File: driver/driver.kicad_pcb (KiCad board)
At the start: 2 copper layers, 100 x 100 mm, 103 parts, among them J1 OUT_A, J10 FAN, J2 OUT_B, J4 RJ45_LED_Shielded, J5 RJ45_LED_Shielded, J6 1602 I2C LCD, J7 IN_VCC, J8 IN_GND, J9 SWD, Q1 TPHR6503PL, Q2 TPHR6503PL, Q3 TPHR6503PL, Q4 TPHR6503PL, U1 MT3608, U10 PC817, U11 AMS1117-5.0, U12 PC817, U13 MAX485E, U2 74HC595, U3 AMS1117-3.3, U4 TC4427, U5 TC4427, U6 STM32F030F4Px, U7 INA226, U8 MCP9804_MSOP, U9 PC817, Y1 8MHz

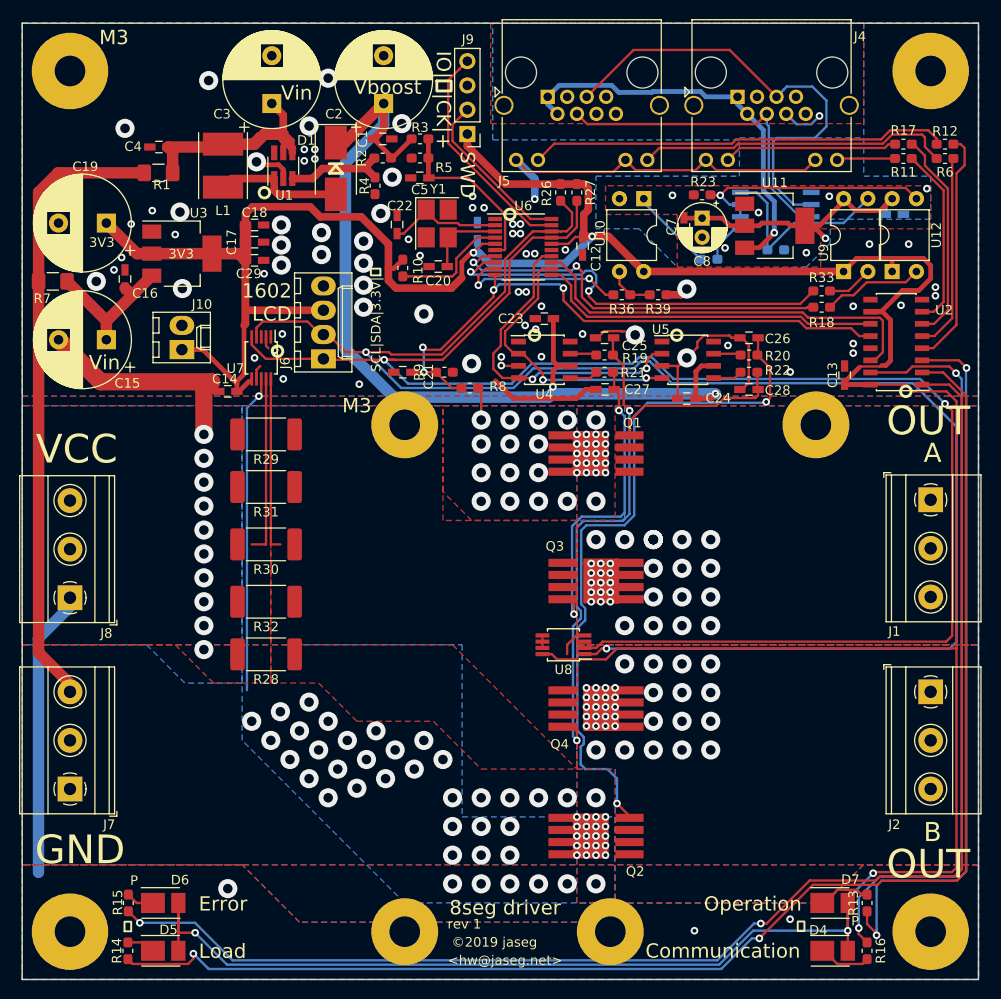
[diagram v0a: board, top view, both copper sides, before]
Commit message: driver: fix a few misplaced vias, set grid origin, fix bottom mask
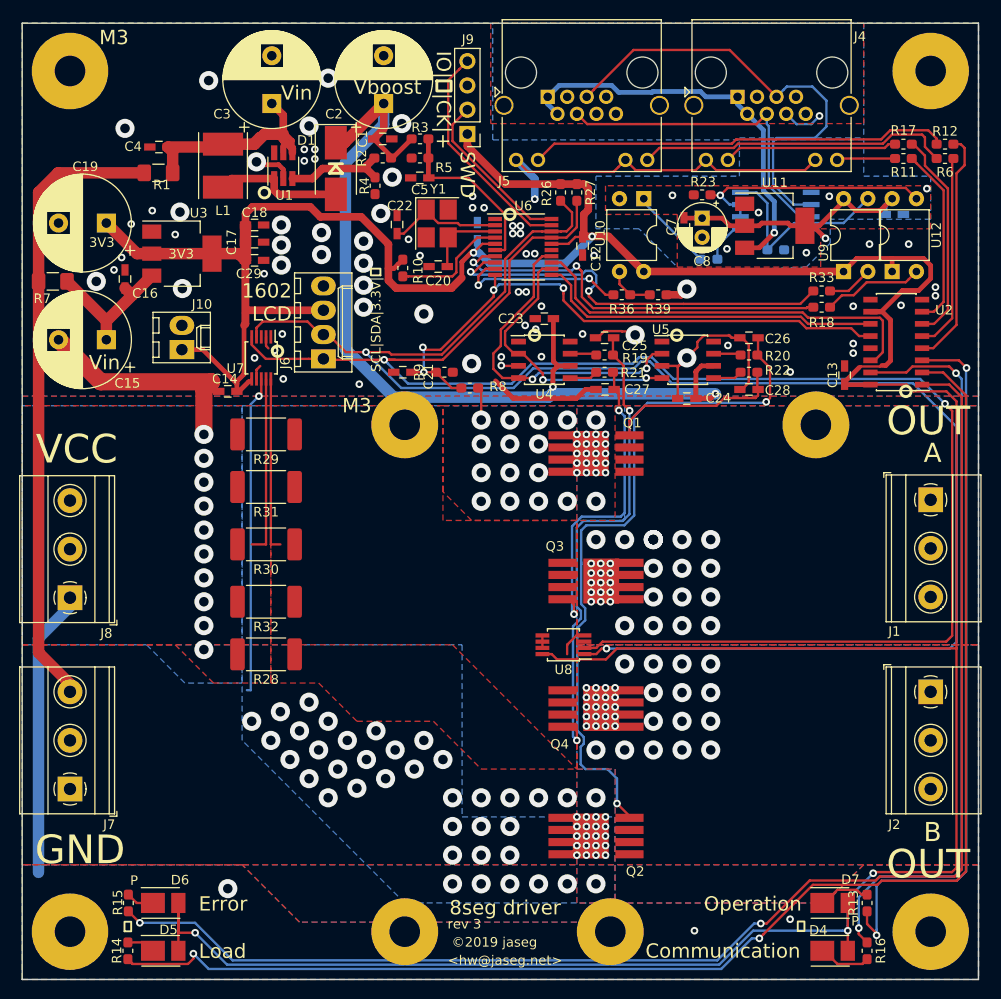
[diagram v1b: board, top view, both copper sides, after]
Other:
- board text added: "rev 3"
- board text removed: "rev 1"
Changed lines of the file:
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@@
     (thickness 1.6)
     (drawings 126)
-    (tracks 1099)
+    (tracks 1100)
     (zones 0)
     (modules 103)
@@
     (user_trace_width 3.2)
     (trace_clearance 0.2)
-    (zone_clearance 0.25)
+    (zone_clearance 0.3)
     (zone_45_only no)
     (trace_min 0.15)
@@
     (solder_mask_min_width 0.25)
     (aux_axis_origin 0 0)
+    (grid_origin 70 55)
     (visible_elements FFFFFF7F)
     (pcbplotparams
-      (layerselection 0x010fc_ffffffff)
+      (layerselection 0x011fc_ffffffff)
       (usegerberextensions false)
       (usegerberattributes false)
@@
       (padsonsilk false)
       (subtractmaskfromsilk false)
-      (outputformat 1)
+      (outputformat 5)
       (mirror false)
-      (drillshape 0)
+      (drillshape 1)
       (scaleselection 1)
-      (outputdirectory "gerber"))
+      (outputdirectory "render"))
   )
   (net 0 "")
@@
   (gr_line (start 90.5 128) (end 79.5 124) (layer B.Mask) (width 2.5))
   (gr_line (start 158 99) (end 165 99) (layer B.Mask) (width 2.5))
-  (gr_text "rev 1" (at 116.238095 149.21) (layer F.SilkS)
+  (gr_text "rev 3" (at 116.238095 149.21) (layer F.SilkS)
     (effects (font (size 1 1) (thickness 0.2)))
   )
@@
   (gr_poly (pts (xy 143 121) (xy 143 132) (xy 129 132) (xy 129 121)) (layer B.Mask) (width 0.15))
   (gr_poly (pts (xy 131.5 106) (xy 131.5 95) (xy 116.5 95) (xy 116.5 106)) (layer B.Mask) (width 0.15))
-  (gr_poly (pts (xy 129 108) (xy 143 108) (xy 143 119) (xy 129 119)) (layer B.Mask) (width 0.15))
+  (gr_poly (pts (xy 129.3 108) (xy 143 108) (xy 143 119) (xy 129.3 119)) (layer B.Mask) (width 0.15))
   (gr_poly (pts (xy 138 121) (xy 143 121) (xy 143 132) (xy 138 132)) (layer F.Mask) (width 0.15))
   (gr_poly (pts (xy 138 109) (xy 142.5 109) (xy 143 109) (xy 143 119) (xy 138 119)) (layer F.Mask) (width 0.15))
@@
   )
   (dimension 5 (width 0.3) (layer Dwgs.User)
-    (gr_text "5.000 mm" (at 62.9 57.5 90) (layer Dwgs.User)
+    (gr_text "5.000 mm" (at 62.9 62 90) (layer Dwgs.User)
       (effects (font (size 1.5 1.5) (thickness 0.3)))
     )
@@
   )
   (dimension 35 (width 0.3) (layer Dwgs.User)
-    (gr_text "35.000 mm" (at 62.9 137.5 90) (layer Dwgs.User)
+    (gr_text "35.000 mm" (at 62.9 130 90) (layer Dwgs.User)
       (effects (font (size 1.5 1.5) (thickness 0.3)))
     )
@@
   (via (at 110.4 77.6) (size 0.8) (drill 0.4) (layers F.Cu B.Cu) (net 2))
   (via (at 111.6 79.3) (size 0.8) (drill 0.4) (layers F.Cu B.Cu) (net 2))
-  (via (at 126.8 78.7) (size 0.8) (drill 0.4) (layers F.Cu B.Cu) (net 2))
-  (via (at 121.3 76) (size 0.8) (drill 0.4) (layers F.Cu B.Cu) (net 2))
-  (via (at 122.1 76) (size 0.8) (drill 0.4) (layers F.Cu B.Cu) (net 2))
+  (via (at 129.8 79.3) (size 0.8) (drill 0.4) (layers F.Cu B.Cu) (net 2))
+  (via (at 121.3 76.2) (size 0.8) (drill 0.4) (layers F.Cu B.Cu) (net 2))
+  (via (at 122.1 76.2) (size 0.8) (drill 0.4) (layers F.Cu B.Cu) (net 2))
   (via (at 121.3 77) (size 0.8) (drill 0.4) (layers F.Cu B.Cu) (net 2))
   (via (at 122.1 77) (size 0.8) (drill 0.4) (layers F.Cu B.Cu) (net 2))
@@
   (via (at 152 79) (size 0.8) (drill 0.4) (layers F.Cu B.Cu) (net 10))
   (via (at 138 73) (size 0.8) (drill 0.4) (layers F.Cu B.Cu) (net 10))
-  (via (at 143.5 78.5) (size 0.8) (drill 0.4) (layers F.Cu B.Cu) (net 10))
+  (via (at 143.7 78.6) (size 0.8) (drill 0.4) (layers F.Cu B.Cu) (net 10))
   (via (at 147 74.8) (size 0.8) (drill 0.4) (layers F.Cu B.Cu) (net 10))
   (via (at 154.4 73.1) (size 0.8) (drill 0.4) (layers F.Cu B.Cu) (net 10))
@@
   (segment (start 95 92.2) (end 95 93.75) (width 0.25) (layer F.Cu) (net 21))
   (segment (start 95 93.75) (end 94.75 94) (width 0.25) (layer F.Cu) (net 21))
-  (segment (start 94.75 94) (end 93.5 95.25) (width 0.25) (layer B.Cu) (net 21))
-  (segment (start 93.5 95.25) (end 93.5 124.75) (width 0.25) (layer B.Cu) (net 21))
   (segment (start 73.75 70.65) (end 82.7625 70.65) (width 1.2) (layer F.Cu) (net 21))
   (segment (start 71.7125 72.6875) (end 73.75 70.65) (width 1.2) (layer F.Cu) (net 21))
@@
   (segment (start 118 93.475) (end 117.675 93.15) (width 0.25) (layer F.Cu) (net 21))
   (segment (start 118 96.5) (end 118 93.475) (width 0.25) (layer F.Cu) (net 21))
+  (segment (start 93.9 124.75) (end 93.5 124.75) (width 0.25) (layer B.Cu) (net 21))
+  (segment (start 94.75 94) (end 93.9 94.85) (width 0.25) (layer B.Cu) (net 21))
+  (segment (start 93.9 94.85) (end 93.9 124.75) (width 0.25) (layer B.Cu) (net 21))
   (segment (start 96 92.2) (end 96 109.5) (width 0.25) (layer F.Cu) (net 22))
   (segment (start 96 109.5) (end 97 109.5) (width 0.25) (layer F.Cu) (net 22))

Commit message: driver: Fix ALL the PCB issues in R3
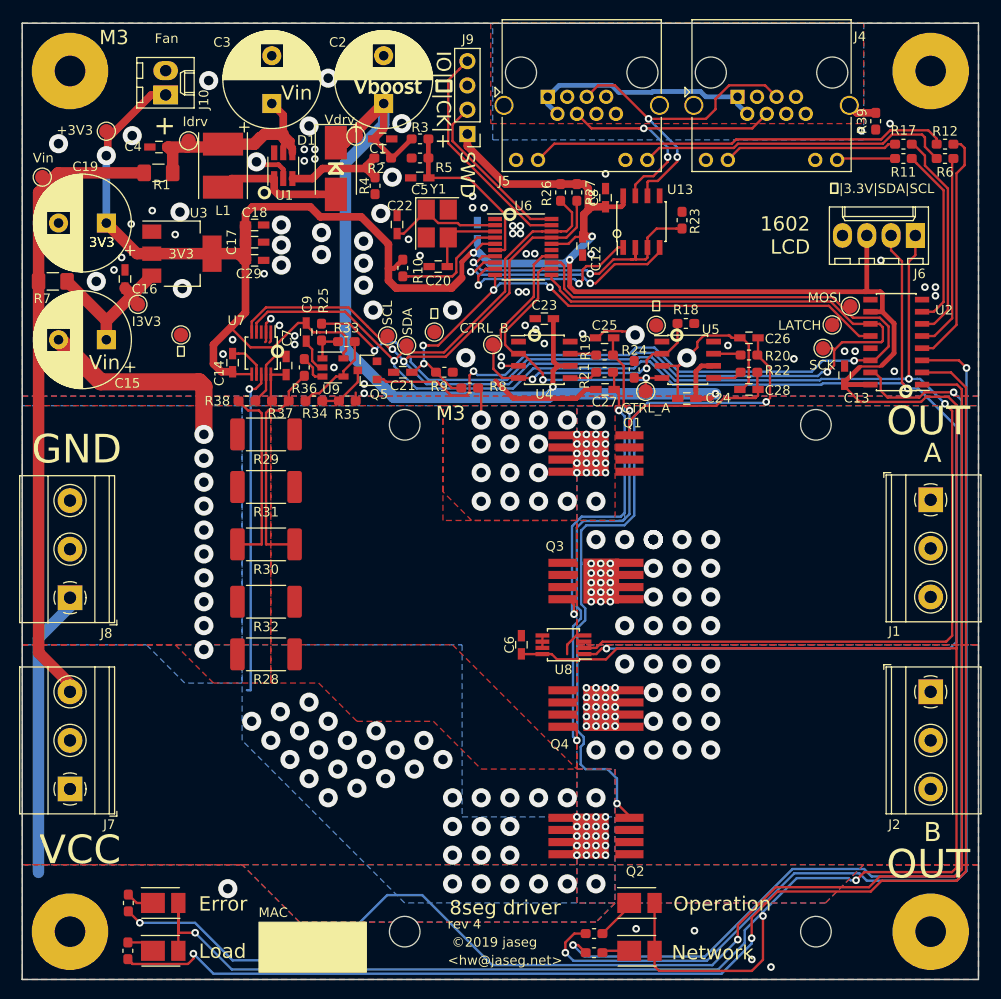
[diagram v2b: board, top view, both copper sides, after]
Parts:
- removed U10, U12: PC817, Package_DIP:DIP-4_W7.62mm
- removed U11: AMS1117-5.0, Package_TO_SOT_SMD:SOT-223-3_TabPin2
- added C9: 100n, Capacitors_SMD:C_0603_HandSoldering, F.Cu at (99.7, 87.3)
- added Q5: AO3400, Package_TO_SOT_SMD:SOT-23, F.Cu at (106.1, 91.3)
- added R24: 1k, Resistor_SMD:R_0603_1608Metric_Pad1.05x0.95mm_HandSolder, F.Cu at (134.0, 91.2)
- added R25: 10k, Resistor_SMD:R_0603_1608Metric_Pad1.05x0.95mm_HandSolder, F.Cu at (101.3, 87.3)
- added R37: 0, Resistor_SMD:R_0603_1608Metric_Pad1.05x0.95mm_HandSolder, F.Cu at (97.0, 94.5)
- added R38: 0, Resistor_SMD:R_0603_1608Metric_Pad1.05x0.95mm_HandSolder, F.Cu at (93.5, 94.5)
- added TP1: Vdrv, TestPoint:TestPoint_Pad_D1.5mm, F.Cu at (104.9, 66.8)
- added TP10: SCL, TestPoint:TestPoint_Pad_D1.5mm, F.Cu at (108.2, 87.7)
- added TP11: SDA, TestPoint:TestPoint_Pad_D1.5mm, F.Cu at (110.2, 88.7)
- added TP12: ⏚, TestPoint:TestPoint_Pad_D1.5mm, F.Cu at (113.1, 87.3)
- added TP13: LATCH, TestPoint:TestPoint_Pad_D1.5mm, F.Cu at (154.7, 86.5)
- added TP14: SCK, TestPoint:TestPoint_Pad_D1.5mm, F.Cu at (153.8, 89.0)
- added TP15: MOSI, TestPoint:TestPoint_Pad_D1.5mm, F.Cu at (156.6, 84.6)
- added TP2: Idrv, TestPoint:TestPoint_Pad_D1.5mm, F.Cu at (87.4, 67.3)
- added TP3: ⏚, TestPoint:TestPoint_Pad_D1.5mm, F.Cu at (86.6, 87.6)
- added TP4: Vin, TestPoint:TestPoint_Pad_D1.5mm, F.Cu at (72.1, 71.1)
- added TP5: I3V3, TestPoint:TestPoint_Pad_D1.5mm, F.Cu at (82.1, 84.4)
- added TP6: +3V3, TestPoint:TestPoint_Pad_D1.5mm, F.Cu at (78.8, 66.3)
- added TP7: CTRL_B, TestPoint:TestPoint_Pad_D1.5mm, F.Cu at (119.2, 88.6)
- added TP8: CTRL_A, TestPoint:TestPoint_Pad_D1.5mm, F.Cu at (135.2, 93.5)
- added TP9: ⏚, TestPoint:TestPoint_Pad_D1.5mm, F.Cu at (136.3, 86.6)
- C6: moved to F.Cu
- C7: value 10u -> 0
- C8: value 22u -> 100n; footprint Capacitor_THT:CP_Radial_D5.0mm_P2.00mm -> Capacitors_SMD:C_0603_HandSoldering
- R18: value 390 -> 1k
- R23: value 720 -> 10k
- R33: value 390 -> 150k
- R34: value 720 -> 100; moved to F.Cu
- R35: value 390 -> 3k6; moved to F.Cu
- R39: value 680 -> 10k
- U13: footprint Package_SO:SO-8_5.3x6.2mm_P1.27mm -> Package_SO:SOIC-8_3.9x4.9mm_P1.27mm; moved to F.Cu
- U9: value PC817 -> NCS325; footprint Package_DIP:DIP-4_W7.62mm -> Package_TO_SOT_SMD:SOT-23-5
- moved J6 63.2 mm to (163.4, 77.2), turned to 180 degrees
- moved C6 59.5 mm to (122.2, 120.0), turned to 90 degrees
- moved U9 54.3 mm to (102.5, 91.0), turned to 0 degrees
- moved R34 50.8 mm to (100.5, 94.5)
- moved R33 50.0 mm to (103.9, 88.3)
- moved C7 44.1 mm to (97.6, 90.8), turned to 90 degrees
- moved R35 40.6 mm to (104.0, 94.5), turned to 0 degrees
- moved R36 34.1 mm to (99.5, 91.0), turned to 270 degrees
- moved R39 29.1 mm to (159.2, 65.2), turned to 90 degrees
- moved R13 28.7 mm to (129.8, 150.2), turned to 0 degrees
- moved R16 28.6 mm to (129.8, 152.2), turned to 0 degrees
- moved J10 26.7 mm to (85.0, 62.5)
- moved H7 21.5 mm to (153.0, 150.0)
- moved D4 20.2 mm to (134.8, 152.0)
- moved D7 20.2 mm to (134.8, 147.0)
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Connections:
- C6 pad 1: /ISO_5V -> +3V3
- C6 pad 2: /ISO_GND -> /GND_MEAS
- C7 pad 1: /ISO_5V -> Net-(C7-Pad1)
- C7 pad 2: /ISO_GND -> Net-(C7-Pad2)
- C8 pad 1: /ISO_5V -> +3V3
- C8 pad 2: /ISO_GND -> GND
- J4 pad 3: /ISO_GND -> /GND_RS485
- J4 pad 6: /ISO_GND -> /GND_RS485
- J4 pad SH: /ISO_GND -> /GND_RS485
- J5 pad 3: /ISO_GND -> /GND_RS485
- J5 pad 6: /ISO_GND -> /GND_RS485
- J5 pad SH: /ISO_GND -> /GND_RS485
- R18 pad 1: /DE -> /CTRL_B
- R18 pad 2: Net-(R18-Pad2) -> GND
- R23 pad 1: /ISO_DE -> /DE
- R23 pad 2: /ISO_GND -> GND
- R33 pad 1: /TX -> /VIsense
- R34 pad 1: /ISO_DI -> Net-(R33-Pad2)
- R34 pad 2: /ISO_GND -> Net-(Q5-Pad3)
- R35 pad 1: /ISO_RO -> Net-(Q5-Pad3)
- R35 pad 2: Net-(R35-Pad2) -> GND
- R36 pad 1: /RX -> Net-(R36-Pad1)
- R36 pad 2: Net-(R36-Pad2) -> /GND_MEAS
- R39 pad 2: Net-(R36-Pad2) -> /GND_RS485
- U13 pad 1: /ISO_RO -> /RX
- U13 pad 2: /ISO_DE -> /DE
- U13 pad 3: /ISO_DE -> /DE
- U13 pad 4: /ISO_DI -> /TX
- U13 pad 5: /ISO_GND -> GND
- U13 pad 8: /ISO_5V -> +3V3
- U7 pad 10: /GND_MEAS -> Net-(C7-Pad1)
- U7 pad 9: GND -> Net-(C7-Pad2)
- U9 pad 1: +3V3 -> /VIsense
- U9 pad 2: Net-(R33-Pad2) -> GND
- U9 pad 3: /ISO_DI -> Net-(R36-Pad1)
- U9 pad 4: /ISO_5V -> Net-(R33-Pad2)
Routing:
- net /SCK: track 36.4 -> 107.0 mm, vias 0 -> 2
- net /MOSI: track 43.4 -> 102.0 mm, vias 0 -> 2
- net +3V3: track 420.7 -> 457.5 mm, vias 5 -> 7
- net GND: track 159.7 -> 126.9 mm, vias 85 -> 91
- net /SLED1: track 75.7 -> 108.0 mm
- net /ISO_5V: track 31.3 -> 0.00 mm, vias 1 -> 0
- net /SLED4: track 78.7 -> 108.2 mm
- net /ISO_DE: track 26.1 -> 0.00 mm, vias 1 -> 0
- net /ISO_DI: track 20.9 -> 0.00 mm
- net /TX: track 43.4 -> 25.0 mm
- net /BUS_VCC: track 42.7 -> 25.3 mm, vias 1 -> 0
- net /SCL: track 173.5 -> 189.7 mm, vias 2 -> 4
- net /SDA: track 176.1 -> 191.5 mm, vias 2 -> 3
- net /RX485_A: track 48.4 -> 35.5 mm, vias 0 -> 2
- net /DE: track 42.0 -> 30.5 mm
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- added copper zone on B.Cu, net /GND_RS485
- added copper zone on F.Cu, net /GND_RS485
- removed copper zone on B.Cu, net /ISO_GND
- removed copper zone on F.Cu, net /ISO_GND
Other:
- board text added: "+"
- board text added: "DATE"
- board text added: "Fan"
- board text added: "IN"
- board text added: "MAC"
- board text added: "Network"
- board text added: "SN"
- board text added: "rev 4"
- board text added: "⏚|3.3V|SDA|SCL"
- board text removed: "Communication"
- board text removed: "P"
- board text removed: "SCL|SDA|3.3V|⏚"
- board text removed: "rev 3"
- board text removed: "⏚"

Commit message: driver: Finish R4 artwork and gerber export
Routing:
- net /SLED3: track 154.7 -> 149.1 mm
- net /SLED1: track 108.0 -> 106.8 mm
- net /SLED4: track 108.2 -> 107.0 mm
